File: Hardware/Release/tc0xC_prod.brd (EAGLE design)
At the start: 101.6 x 99.3 mm, 102 parts, among them IC1 AP2112M-3.3TRG1, Q1 2.5A/30V, Q2 MBT3904DW1T1, Q3 600mA/40V, Q4 MBT3904DW1T1, U2 ESP3212, U4 FT231XS, U5 W25Q32FVSS, Y1 26MHz, Y2 32.768kHz

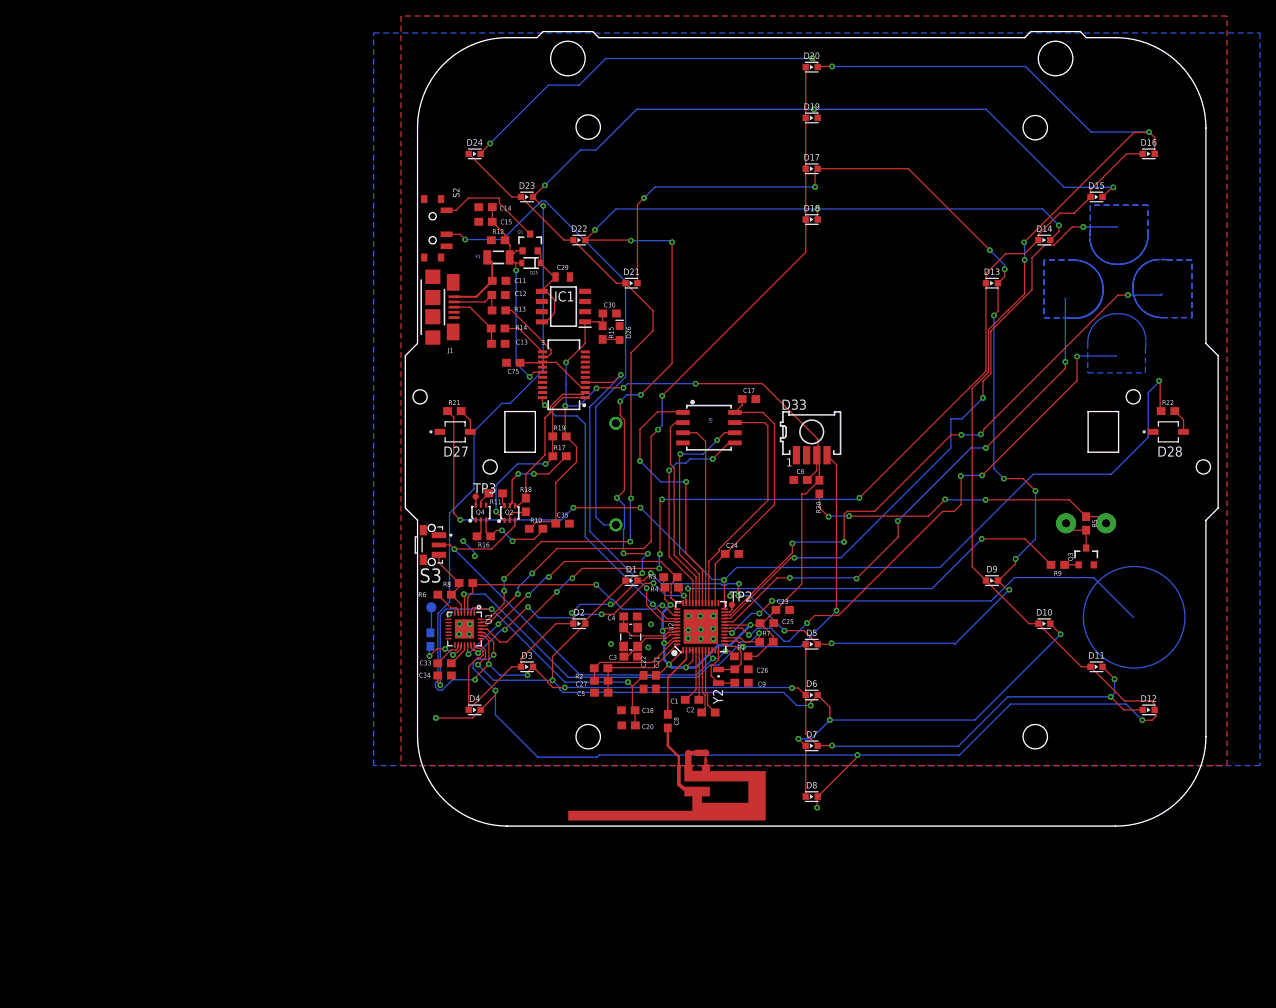
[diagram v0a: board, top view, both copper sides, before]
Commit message: updates for new housing design
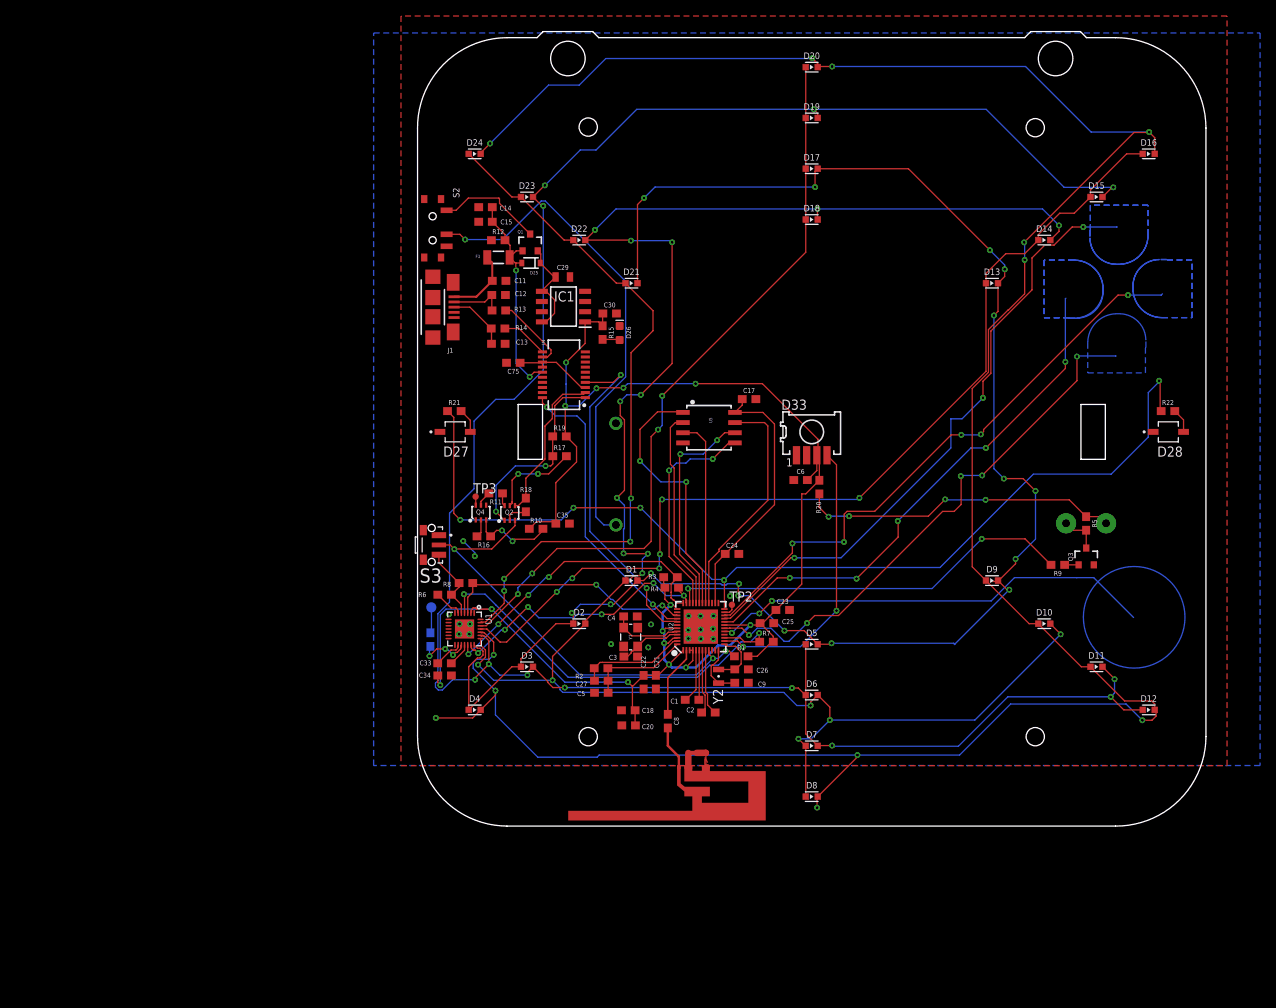
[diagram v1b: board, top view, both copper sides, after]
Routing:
- net CA3: track 269.0 -> 269.8 mm
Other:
- board size 101.6 x 99.3 mm -> 98.6 x 99.3 mm

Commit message: add silk. update layout to fit plastics. minor adjustments to layout.
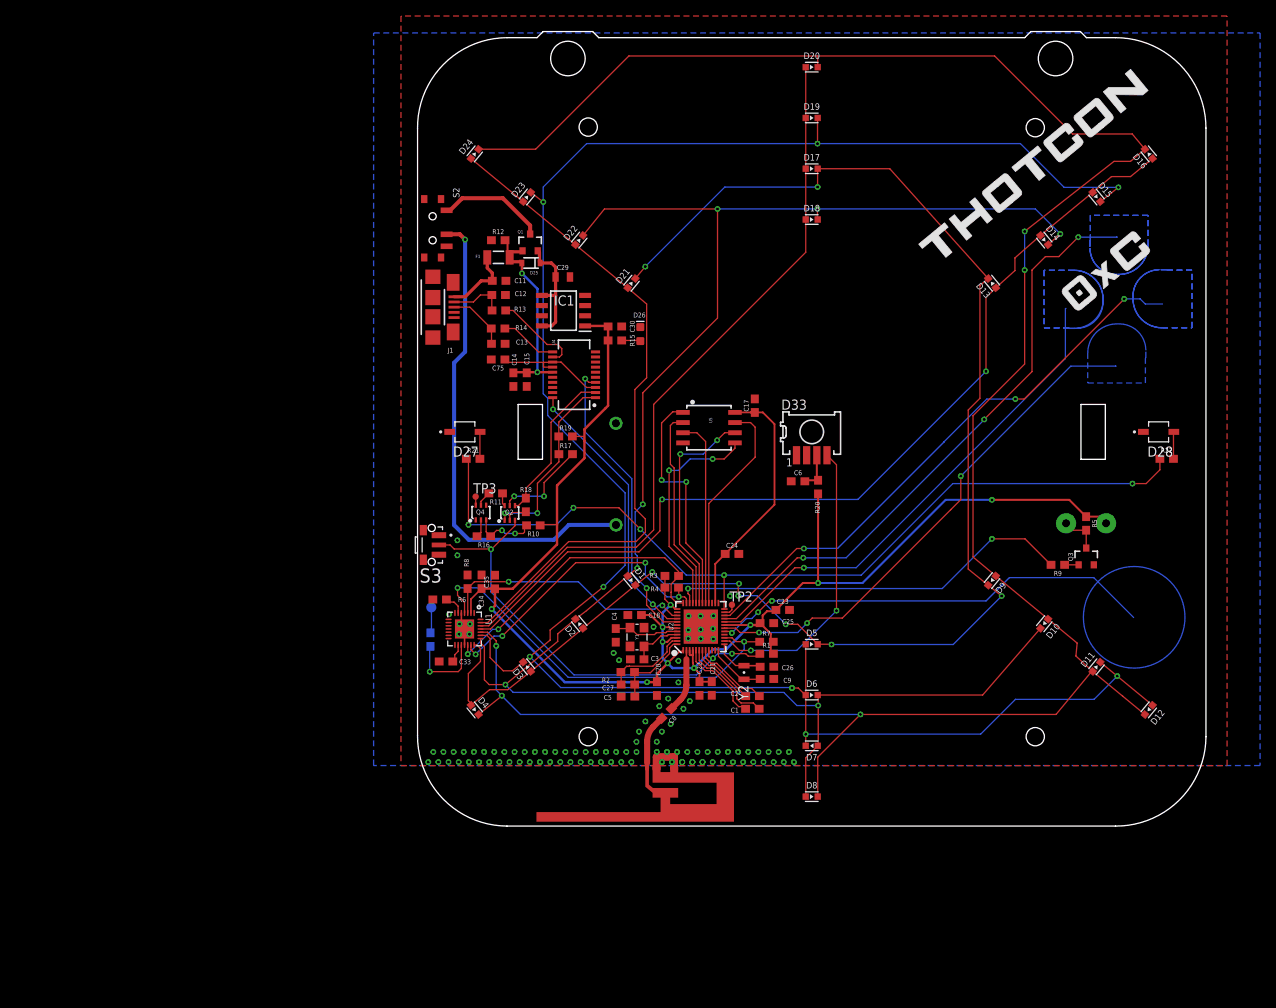
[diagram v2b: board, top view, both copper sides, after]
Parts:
- moved C14 21.8 mm to (13.5, 57.3), turned to 270 degrees
- moved C15 20.4 mm to (15.2, 57.3), turned to 270 degrees
- moved C34 12.6 mm to (9.53, 32.1), turned to 90 degrees
- moved C18 11.9 mm to (28.7, 27.9)
- moved C35 11.2 mm to (11.2, 32.0), turned to 90 degrees
- moved C1 7.62 mm to (43.4, 16.2)
- moved C21 7.03 mm to (38.3, 18.7)
- moved C22 7.03 mm to (36.8, 18.7)
- moved R21 6.41 mm to (8.47, 47.4)
- moved R22 5.97 mm to (95.2, 47.4)
- moved C2 5.89 mm to (43.4, 17.8)
- moved C20 5.80 mm to (31.5, 18.7), turned to 270 degrees
- moved E1 3.97 mm to (30.2, 8.98)
- moved R2 3.37 mm to (27.8, 20.8)
- moved C27 3.37 mm to (27.8, 19.2)
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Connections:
- new net N$17: C6.2, D33.3, R20.1
- net 3.3V: no longer C6.2, D33.3, R20.1
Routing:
- net 3.3V: track 241.1 -> 197.3 mm, vias 18 -> 10
- net CA4: track 313.2 -> 289.8 mm, vias 12 -> 5
- net CA1: track 205.9 -> 188.5 mm, vias 16 -> 8
- net IR_OUT: track 127.2 -> 110.2 mm
- net CA2: track 245.3 -> 230.9 mm, vias 17 -> 7
- net GND: track 21.7 -> 9.19 mm, vias 20 -> 105
- net CA3: track 269.8 -> 262.5 mm, vias 12 -> 8
- net 37: track 6.21 -> 11.8 mm
- net CA5: track 121.7 -> 116.1 mm, vias 6 -> 2
- net U0TXD: track 42.8 -> 37.6 mm
- net N$17: track 0.00 -> 4.90 mm
- net 3.3V_F: track 10.1 -> 14.5 mm
- net T_DOWN: track 69.0 -> 64.7 mm, vias 5 -> 3
- net N$11: track 6.66 -> 10.2 mm, vias 3 -> 1
- net 36: track 7.20 -> 10.8 mm
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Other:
- board text added: "OFF"
- board text added: "ON"
- board text added: "RESET"

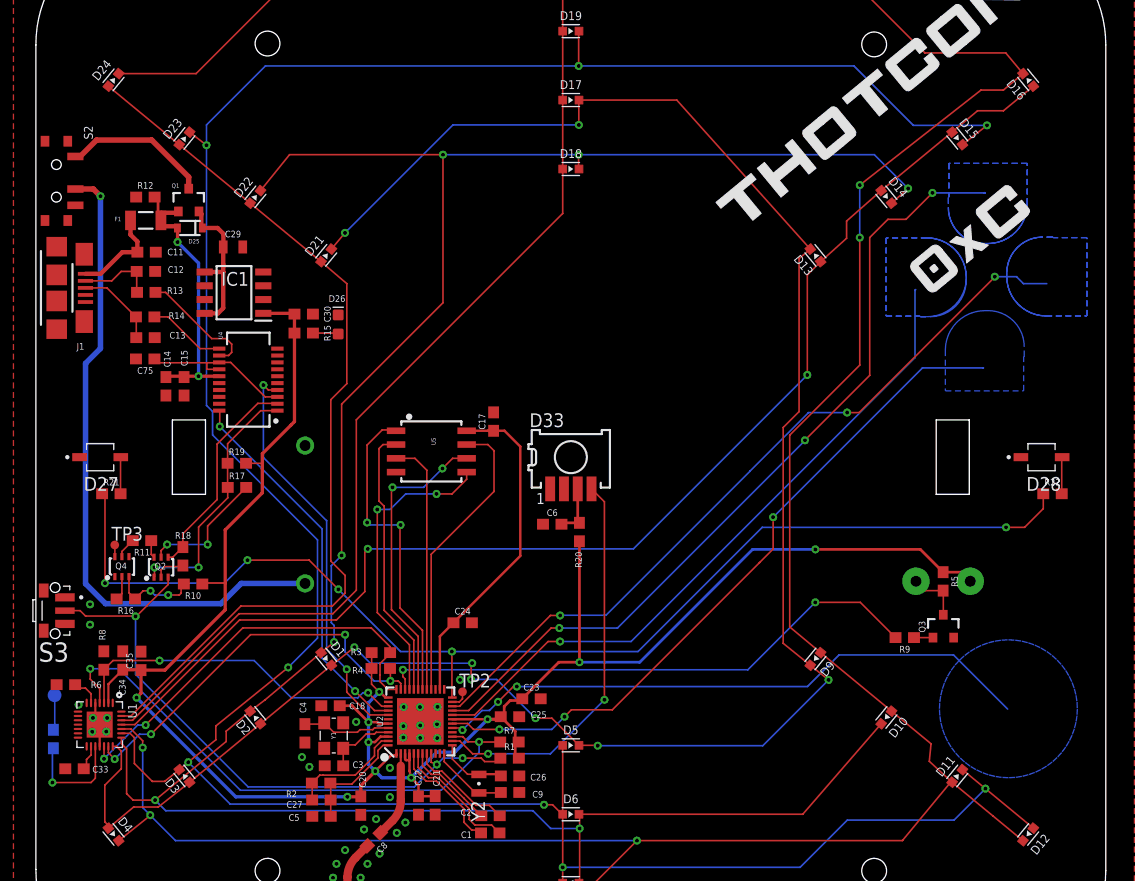
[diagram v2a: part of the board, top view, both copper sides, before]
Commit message: update cutouts and keepout. minor routing adjustments.
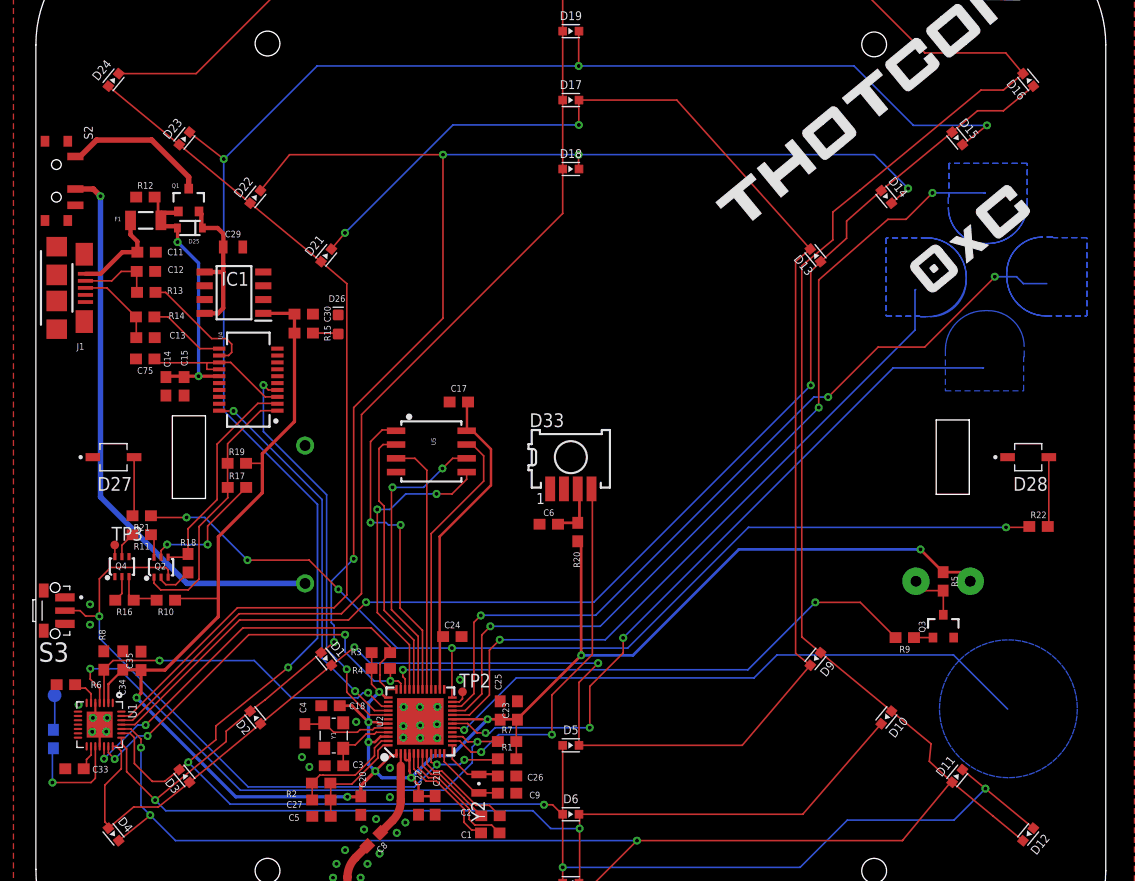
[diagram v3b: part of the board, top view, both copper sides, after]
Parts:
- moved C17 3.68 mm to (40.5, 55.9), turned to 180 degrees
- moved R21 3.46 mm to (11.3, 45.4), turned to 180 degrees
- moved R22 3.28 mm to (93.9, 44.4)
- moved R10 2.92 mm to (13.5, 37.6)
- moved C23 1.68 mm to (45.9, 27.5), turned to 90 degrees
- moved C24 1.59 mm to (39.9, 34.3)
- moved D27 1.23 mm to (8.67, 50.8)
- moved D28 1.23 mm to (92.9, 50.8)
- moved C25 1.07 mm to (44.3, 27.5), turned to 90 degrees
- moved R18 0.79 mm to (15.5, 41.0)
- moved R11 0.54 mm to (11.3, 43.7)
- moved C6 0.32 mm to (48.8, 44.6)
- moved C9 0.28 mm to (44.9, 19.8)
- moved C26 0.27 mm to (44.9, 21.4)
- moved R1 0.24 mm to (44.9, 23.0)
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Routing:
- net IR_OUT: track 110.2 -> 95.2 mm
- net N$16: track 60.6 -> 52.4 mm
- net T_LEFT: track 71.4 -> 75.3 mm
- net CHIP_PU: track 57.6 -> 61.2 mm
- net N$13: track 8.02 -> 4.59 mm, vias 2 -> 0
- net N$6: track 3.39 -> 6.43 mm
- net T_UP: track 76.3 -> 78.7 mm
- net N$5: track 3.38 -> 5.46 mm
- net CA3: track 262.5 -> 260.5 mm
- net ACC_INT: track 36.5 -> 34.5 mm
- net CA1: track 188.5 -> 190.5 mm, vias 8 -> 4
- net FLASH_SHD: track 27.1 -> 25.5 mm
- net T_DOWN: track 64.7 -> 66.3 mm
- net FLASH_VDD: track 31.5 -> 30.0 mm
- net DTR: track 23.3 -> 24.8 mm, vias 2 -> 0
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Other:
- outline, holes or cut-outs redrawn

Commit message: small layout adjustments
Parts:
- moved R1 37.4 mm to (9.68, 35.4)
- moved R7 33.2 mm to (13.5, 35.4)
- moved C23 13.4 mm to (33.3, 32.2), turned to 0 degrees
- moved C17 5.08 mm to (40.5, 50.8)
- moved U5 5.08 mm to (38.0, 46.2)
- moved R2 3.01 mm to (30.0, 18.7), turned to 270 degrees
- moved R3 2.61 mm to (33.3, 35.4)
- moved R4 2.48 mm to (33.3, 33.8)
- moved C1 2.01 mm to (44.6, 17.8)
- moved C2 2.00 mm to (44.6, 19.4)
- moved C26 1.62 mm to (44.6, 23.0)
- moved Y2 1.62 mm to (42.0, 22.3)
- moved C9 1.62 mm to (44.6, 21.4)
- moved C5 1.33 mm to (26.9, 18.7), turned to 270 degrees
- moved C8 1.27 mm to (32.6, 14.3)
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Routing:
- net 3.3V: track 197.2 -> 207.0 mm, vias 10 -> 9
- net FLASH_SCS: track 29.2 -> 21.5 mm
- net N$16: track 52.4 -> 46.1 mm
- net FLASH_SCK: track 27.6 -> 21.9 mm
- net CA1: track 190.5 -> 185.0 mm
- net FLASH_SDI: track 27.8 -> 22.5 mm
- net FLASH_VDD: track 30.0 -> 24.9 mm
- net FLASH_SWP: track 23.5 -> 18.4 mm
- net FLASH_SDO: track 25.2 -> 20.2 mm
- net FLASH_SHD: track 25.5 -> 20.4 mm
- net SCL: track 37.0 -> 42.0 mm, vias 4 -> 2
- net DST: track 50.9 -> 55.5 mm
- net CHIP_PU: track 61.2 -> 56.8 mm, vias 3 -> 2
- net SDA: track 38.6 -> 43.0 mm
- net BUZZER_OUT: track 51.2 -> 54.3 mm
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
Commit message: updated dimension around lanyard holes
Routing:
- net CA2: track 227.5 -> 236.3 mm
- net BUZZER_OUT: track 54.3 -> 51.7 mm
- net CA1: track 185.0 -> 185.7 mm
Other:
- board size 98.6 x 99.3 mm -> 98.6 x 99.6 mm

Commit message: Review CAMS, Art, Schematic Updates - Pre final route
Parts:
- added D29, D30: VSMB2020X01, VSMB2020X01:DIO_VSMB2020X01
- added R23, R24: 8.2, SparkFun-Resistors:0603
- added U$1, U$4: T2N7002BK, T2N7002BK:SOT-23/E0-95/B0-4
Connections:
- new net N$19: D29.C, U$1.3
- new net N$20: D30.C, U$4.3
- new net N$21: D29.A, R23.2
- new net N$22: D30.A, R24.2
- net 3.3V: now also R23.1, R24.1
- net GND: now also U$1.2, U$4.2
- net IR_OUT: now also U$1.1, U$4.1
